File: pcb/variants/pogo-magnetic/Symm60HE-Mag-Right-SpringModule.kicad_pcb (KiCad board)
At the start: 2 copper layers, 32 x 18 mm, 2 parts

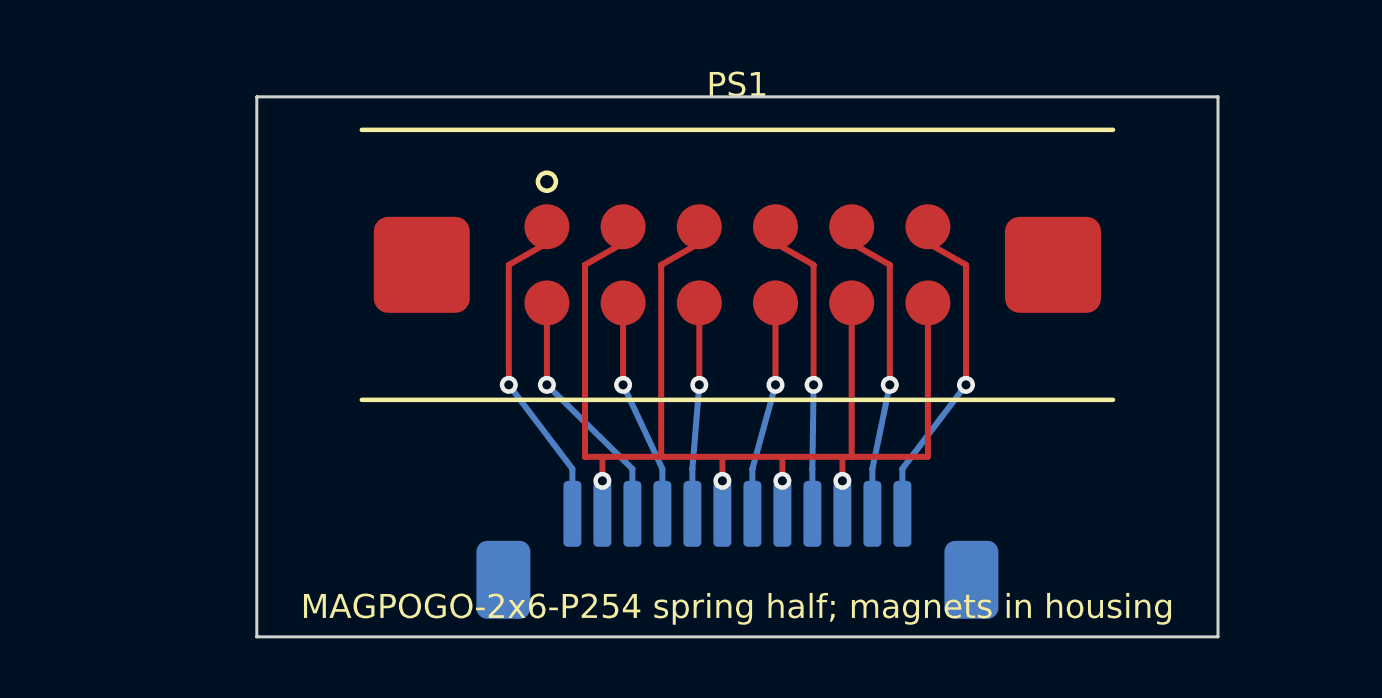
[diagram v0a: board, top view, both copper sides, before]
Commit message: Rebuild the magnetic variant around SUNMON 903-00081
Replaces the invented MAGPOGO-2x6-P254 interface drawing with a real part:
SUNMON 903-00081 / 904-00080 (MC142-09R), nine contacts in two staggered rows
on 1.50 mm pitch with 1.25 mm between rows, 1.20 mm contacts, 0.50 mm DIP
tails, and N52 magnets internal to the housing keyed N to S. Every footprint
dimension is read off the two published drawings.

Nine contacts is the link's functional minimum -- four ADC channels, three mux
selects, +3V3A and one ground -- so the twelve-way interface's four separate
grounds collapse to one and the module ties the controller ZIF's four ground
pads to that single contact.

The stagger is the hard part and it is the part's, not this attempt's:
diagonal neighbours are 1.458 mm apart with 1.25 mm pads, so nothing routes
between the contacts and every run leaves the array at its perimeter. The row
facing the ZIF drops straight to B.Cu; the other takes F.Cu over the top, down
the module side and back in above the ZIF.

Routing is not finished: 6 and 4 clearance flags on the modules, 11 on each
half. Recorded in the README along with why. Footprints, land pattern, pinout
and module outline are settled; the fanout is not.

Modules are 26 x 16 mm. docs/img/42 redraws them and docs/img/43 adds the
target breakout on the Hall PCBs.

Co-Authored-By: Claude Opus 5 <noreply@anthropic.com>
Claude-Session: https://claude.ai/code/session_01CRkZ4zVz5Mq7Fa3C5HAmii
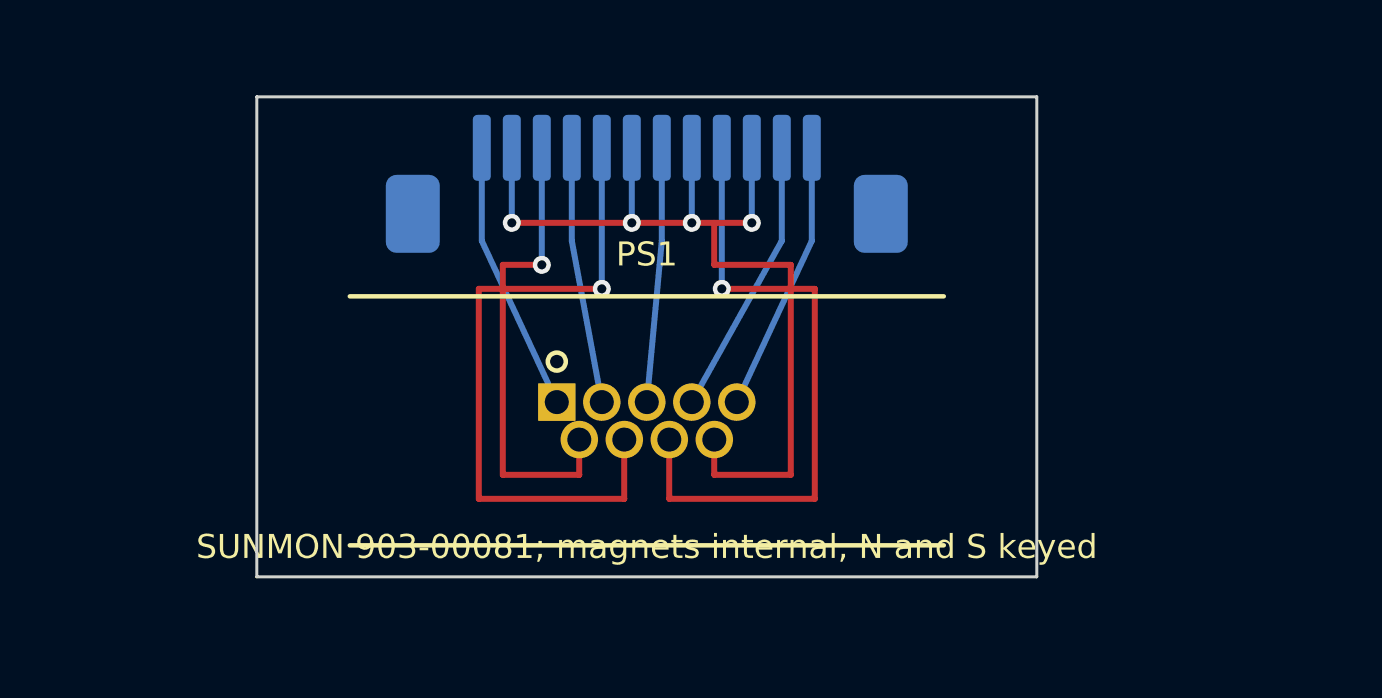
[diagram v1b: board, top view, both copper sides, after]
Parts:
- PS1: value MAGPOGO-2x6-P254-S -> 903-00081; footprint MagPogo_2x6_P254_Spring -> MagPogo_9_MC142_Spring
- moved JF1 12.6 mm to (13.0, 2.80)
- moved PS1 6.01 mm to (13.0, 10.8)
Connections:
- PS1 pad 2: GND -> MUX_A1
- PS1 pad 3: GND -> ADC_R1
- PS1 pad 4: ADC_R2 -> ADC_R3
- PS1 pad 5: ADC_R3 -> ADC_R4
- PS1 pad 6: ADC_R4 -> MUX_A0
- PS1 pad 7: MUX_A0 -> MUX_A2
- PS1 pad 8: MUX_A1 -> ADC_R2
- PS1 pad 9: MUX_A2 -> GND
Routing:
- net MUX_A2: track 7.04 -> 22.6 mm
- net GND: track 46.1 -> 32.7 mm
- net ADC_R2: track 10.3 -> 21.6 mm
- net MUX_A0: track 8.23 -> 15.9 mm
- net ADC_R4: track 11.0 -> 9.03 mm, vias 1 -> 0
- net +3V3A: track 11.0 -> 9.03 mm, vias 1 -> 0
- net ADC_R1: track 7.13 -> 8.50 mm, vias 1 -> 0
- net MUX_A1: track 7.32 -> 8.57 mm, vias 1 -> 0
- net ADC_R3: track 10.4 -> 9.26 mm, vias 1 -> 0
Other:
- board size 32 x 18 mm -> 26 x 16 mm
- board text added: "SUNMON 903-00081; magnets internal, N and S keyed"
- board text removed: "MAGPOGO-2x6-P254 spring half; magnets in housing"
